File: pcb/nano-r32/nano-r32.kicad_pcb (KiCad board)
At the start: 2 copper layers, 24 x 45 mm, 16 parts, among them J1 USB_A, J2 Conn_01x14_Pin, J3 Conn_01x14_Pin, U1 CH32X035G8R6

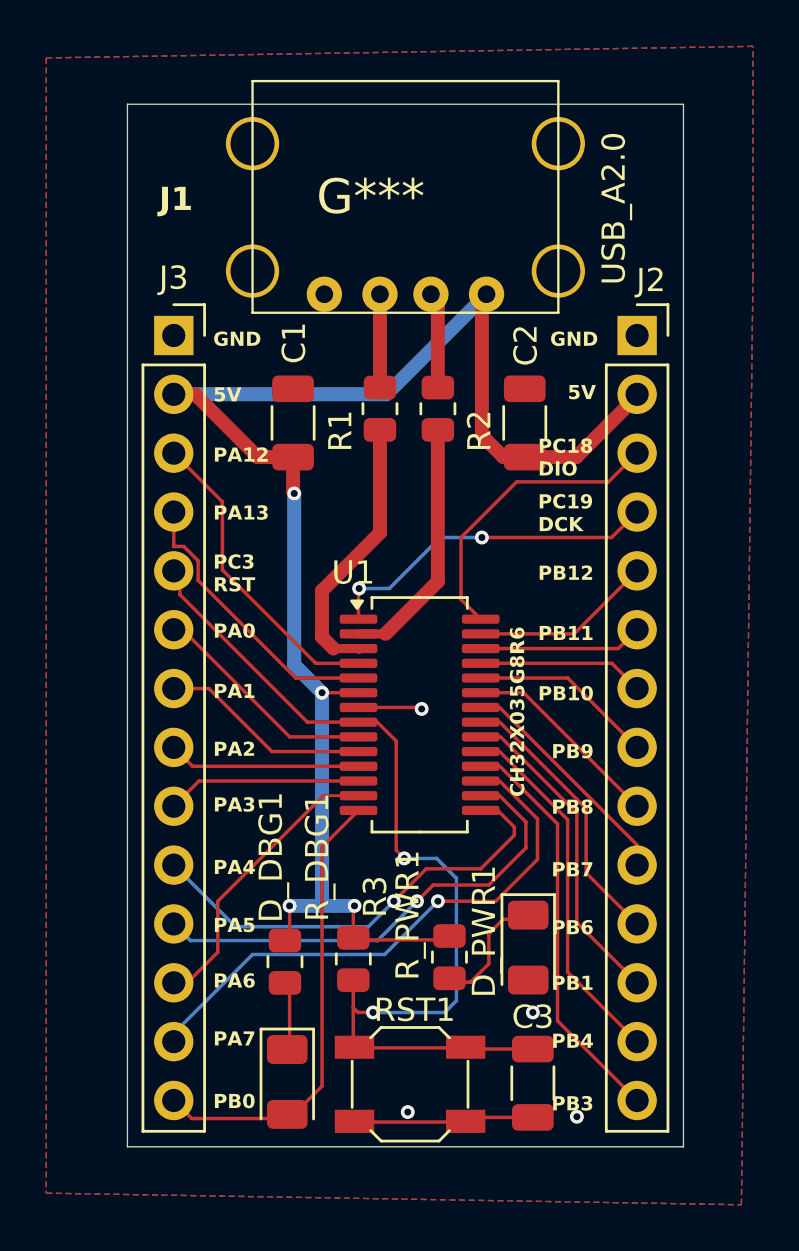
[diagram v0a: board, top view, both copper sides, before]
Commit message: update debug board schematic and layout: add boot button, fix led polarity
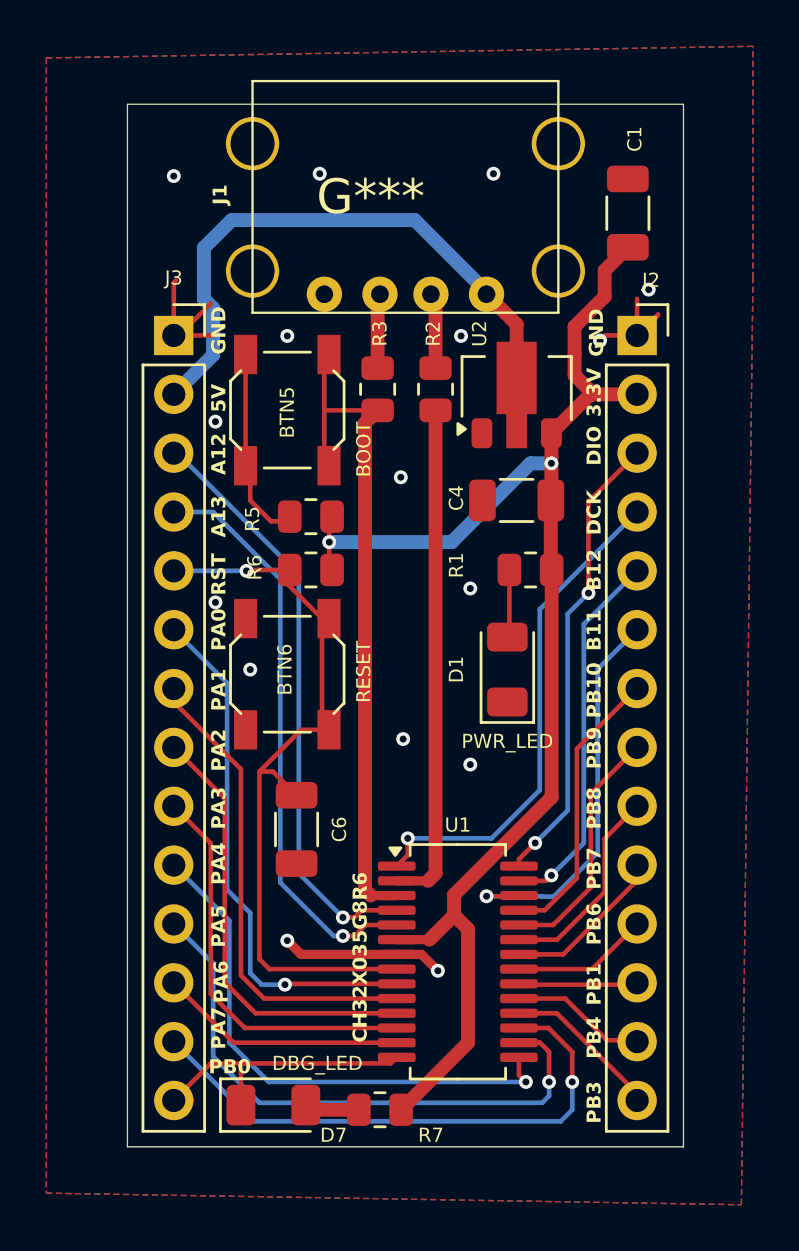
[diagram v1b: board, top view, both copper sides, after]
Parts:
- removed C2: 10u, Capacitor_SMD:C_1206_3216Metric
- removed C3: 100n, Capacitor_SMD:C_1206_3216Metric
- removed D_DBG1, D_PWR1: LED, Diode_SMD:D_1206_3216Metric
- removed RST1: SW_Push, Button_Switch_SMD:SW_SPST_5x5x1.5
- removed R_DBG1, R_PWR1: 330R, Resistor_SMD:R_0805_2012Metric
- added BTN5: SW_Push, Button_Switch_SMD:SW_SPST_5x5x1.5, F.Cu at (72.9, 68.2)
- added BTN6: SW_Push, Button_Switch_SMD:SW_SPST_5x5x1.5, F.Cu at (72.9, 79.6)
- added C4: 100n, Capacitor_SMD:C_1206_3216Metric, F.Cu at (82.8, 72.1)
- added C6: 100n, Capacitor_SMD:C_1206_3216Metric, F.Cu at (73.3, 86.3)
- added D1: LED, Diode_SMD:D_1206_3216Metric, F.Cu at (82.4, 79.4)
- added D7: LED, Diode_SMD:D_1206_3216Metric, F.Cu at (72.3, 98.2)
- added R5: 5.1K, Resistor_SMD:R_0805_2012Metric, F.Cu at (73.9, 72.8)
- added R6: 5.1K, Resistor_SMD:R_0805_2012Metric, F.Cu at (73.9, 75.1)
- added R7: 330R, Resistor_SMD:R_0805_2012Metric, F.Cu at (76.9, 98.4)
- added U2: HT75xx-1-SOT89, Package_TO_SOT_SMD:SOT-89-3, F.Cu at (82.8, 67.2)
- C1: value 100n -> 10u
- R1: value 22R -> 330R
- R3: value 5.1K -> 22R
- moved R3 24.6 mm to (76.8, 67.3)
- moved C1 17.1 mm to (87.6, 59.7), turned to -90 degrees
- moved U1 10.8 mm to (80.3, 92.0)
- moved R1 8.03 mm to (83.4, 75.1), turned to 180 degrees
- moved R2 2.54 mm to (79.3, 67.3), turned to 90 degrees
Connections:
- C1 pad 1: +5V -> GND
- C1 pad 2: GND -> Net-(J2-Pin_2)
- J2 pad 2: +5V -> Net-(J2-Pin_2)
- R1 pad 1: Net-(U1-PC16/UDM/T1C4/TX4_/I2C_/RX4_/CTS1/PC11) -> Net-(J2-Pin_2)
- R1 pad 2: Net-(J1-D-) -> Net-(D1-A)
- R2 pad 1: Net-(J1-D+) -> Net-(U1-PC16/UDM/T1C4/TX4_/I2C_/RX4_/CTS1/PC11)
- R2 pad 2: Net-(U1-PC17/UDP/RTS1/TX4_/I2C_/RX4_/T1ET/PC10) -> Net-(J1-D-)
- R3 pad 1: +5V -> Net-(J1-D+)
- R3 pad 2: Net-(J3-Pin_5) -> Net-(U1-PC17/UDP/RTS1/TX4_/I2C_/RX4_/T1ET/PC10)
- U1 pad 6: +5V -> Net-(J2-Pin_2)
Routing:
- net Net-(J2-Pin_2): track 0.00 -> 60.5 mm, vias 0 -> 2
- net +5V: track 66.9 -> 28.0 mm, vias 4 -> 0
- net Net-(U1-PC17/UDP/RTS1/TX4_/I2C_/RX4_/T1ET/PC10): track 12.4 -> 29.5 mm
- net Net-(J3-Pin_4): track 12.3 -> 25.6 mm, vias 0 -> 1
- net Net-(J3-Pin_6): track 9.89 -> 23.1 mm, vias 0 -> 1
- net Net-(J3-Pin_3): track 13.5 -> 25.6 mm, vias 0 -> 1
- net Net-(J3-Pin_7): track 9.10 -> 20.7 mm
- net Net-(U1-PC16/UDM/T1C4/TX4_/I2C_/RX4_/CTS1/PC11): track 10.9 -> 21.8 mm
- net Net-(J2-Pin_14): track 17.7 -> 6.84 mm
- net Net-(J3-Pin_8): track 8.31 -> 19.0 mm
- net Net-(J2-Pin_6): track 7.09 -> 17.3 mm, vias 0 -> 1
- net Net-(J2-Pin_13): track 15.8 -> 5.79 mm
- net Net-(J3-Pin_5): track 41.8 -> 32.6 mm, vias 2 -> 1
- net Net-(J3-Pin_9): track 8.43 -> 17.4 mm
- net Net-(J2-Pin_12): track 13.9 -> 5.15 mm
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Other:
- board text added: "3.3V"
- board text added: "A12"
- board text added: "A13"
- board text added: "B11"
- board text added: "B12"
- board text added: "BOOT"
- board text added: "DBG_LED"
- board text added: "DCK"
- board text added: "DIO"
- board text added: "PWR_LED"
- board text added: "RESET"
- board text added: "RST"
- board text added: "rev. 20250328"
- board text removed: "PA12"
- board text removed: "PA13"
- board text removed: "PB11"
- board text removed: "PB12"
- board text removed: "PC16"
- board text removed: "PC17"
- board text removed: "PC18 DIO"
- board text removed: "PC19 DCK"
- board text removed: "PC3 RST"
- board text removed: "USB_A2.0"
